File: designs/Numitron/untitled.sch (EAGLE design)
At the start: 10 parts, among them IC2 TLC5916IN, IC3 TLC5916IN, IC4 TLC5916IN, IC5 TLC5916IN

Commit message: added designs Numitron modular first finish review tomorrow or tuesday
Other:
- moved on the sheet: 1, 2, 3, 4, IC2, IC3, IC4, IC5, R1, SV1

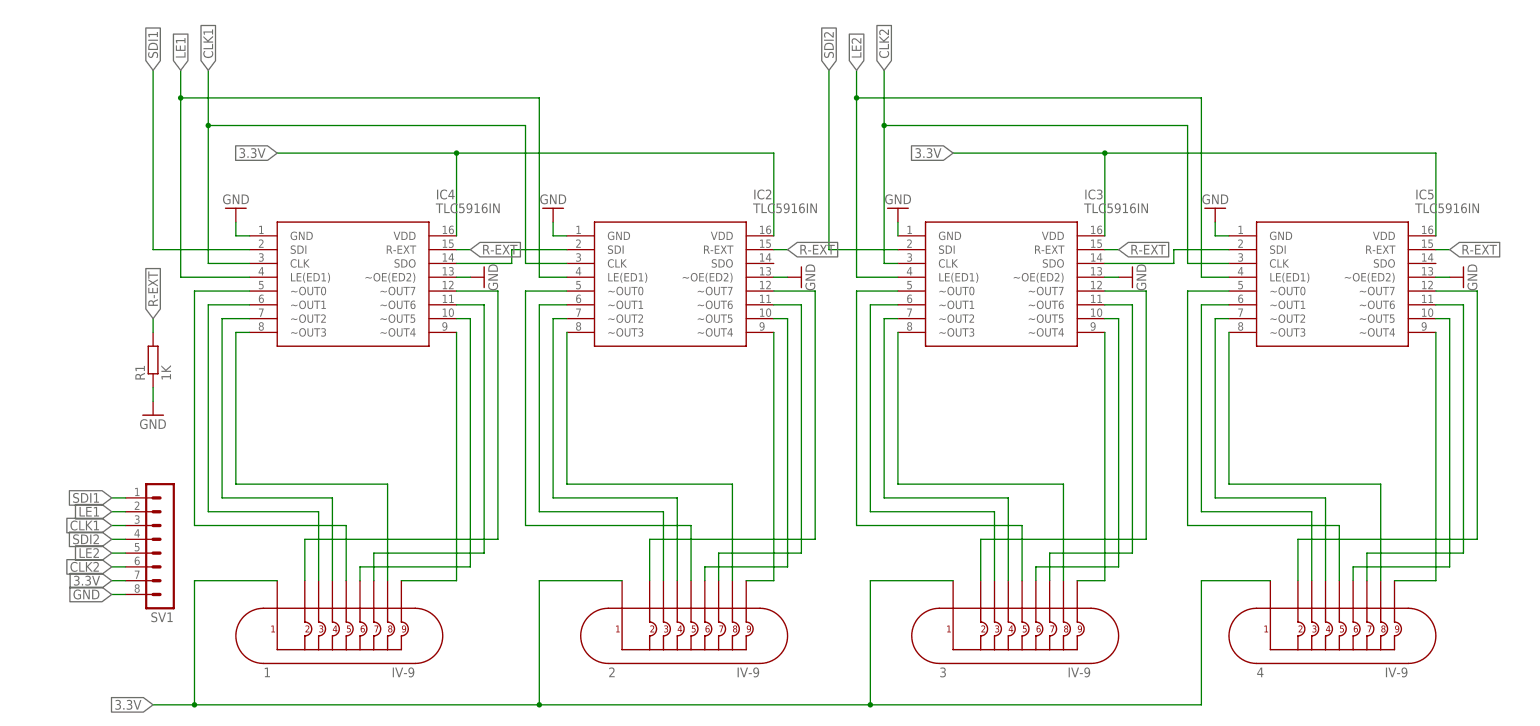
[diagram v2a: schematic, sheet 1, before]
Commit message: numitron 4 resistor error correction
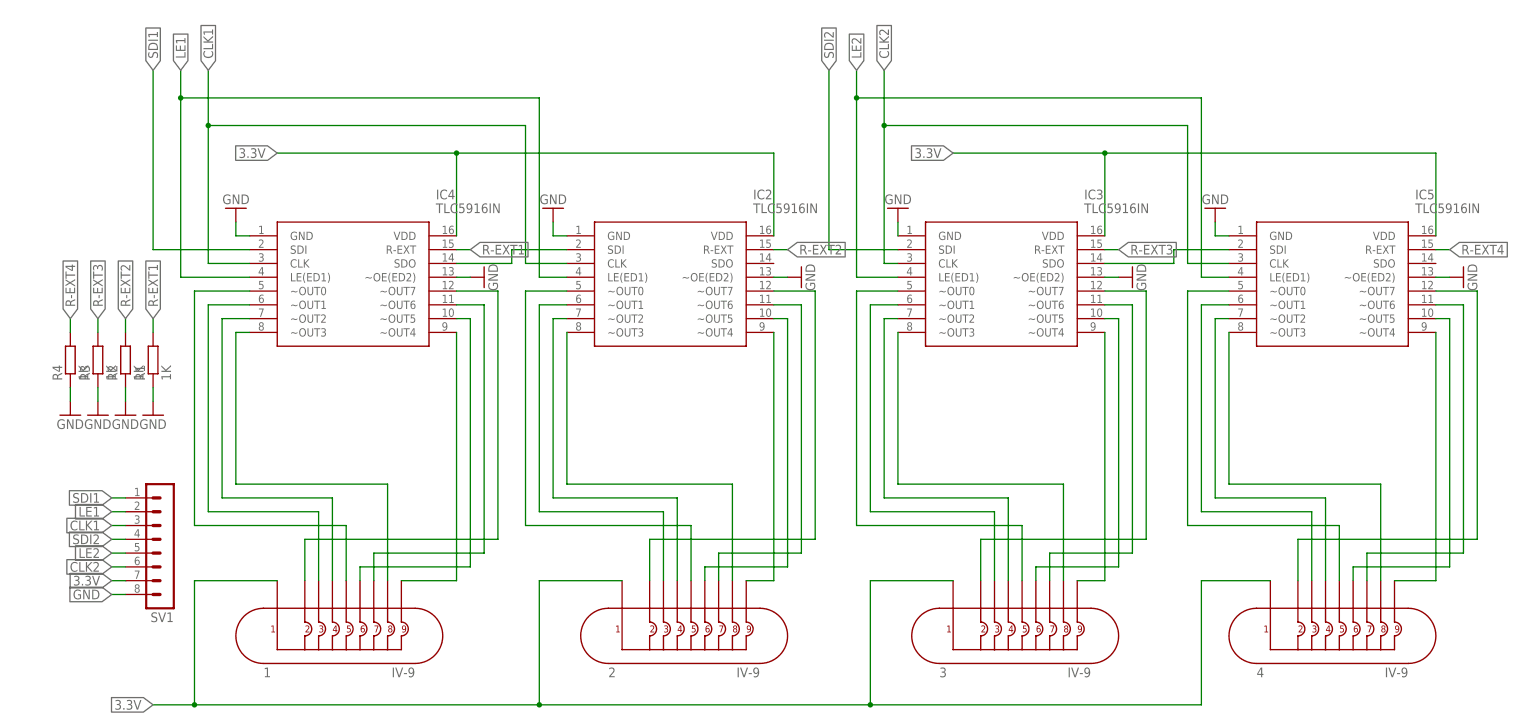
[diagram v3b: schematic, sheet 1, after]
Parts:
- added R2, R3, R4: 1K, rcl:R-EU_R1206
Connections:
- removed net R-EXT: IC2.R-EXT, IC3.R-EXT, IC4.R-EXT, IC5.R-EXT, R1.2
- new net R-EXT1: IC4.R-EXT, R1.2
- new net R-EXT2: IC2.R-EXT, R2.2
- new net R-EXT3: IC3.R-EXT, R3.2
- new net R-EXT4: IC5.R-EXT, R4.2
- net GND: now also R2.1, R3.1, R4.1
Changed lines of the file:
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@@
 <?xml version="1.0" encoding="utf-8"?>
 <!DOCTYPE eagle SYSTEM "eagle.dtd">
-<eagle version="9.5.1">
+<eagle version="9.4.2">
 <drawing>
 <settings>
@@
 <part name="GND12" library="supply1" library_urn="urn:adsk.eagle:library:371" deviceset="GND" device=""/>
 <part name="SV1" library="con-lstb" library_urn="urn:adsk.eagle:library:162" deviceset="MA08-1" device="" package3d_urn="urn:adsk.eagle:package:8343/1"/>
+<part name="R2" library="rcl" library_urn="urn:adsk.eagle:library:334" deviceset="R-EU_" device="R1206" package3d_urn="urn:adsk.eagle:package:23540/2" value="1K"/>
+<part name="GND9" library="supply1" library_urn="urn:adsk.eagle:library:371" deviceset="GND" device=""/>
+<part name="R3" library="rcl" library_urn="urn:adsk.eagle:library:334" deviceset="R-EU_" device="R1206" package3d_urn="urn:adsk.eagle:package:23540/2" value="1K"/>
+<part name="GND10" library="supply1" library_urn="urn:adsk.eagle:library:371" deviceset="GND" device=""/>
+<part name="R4" library="rcl" library_urn="urn:adsk.eagle:library:334" deviceset="R-EU_" device="R1206" package3d_urn="urn:adsk.eagle:package:23540/2" value="1K"/>
+<part name="GND11" library="supply1" library_urn="urn:adsk.eagle:library:371" deviceset="GND" device=""/>
 </parts>
 <sheets>
@@
 <attribute name="NAME" x="26.67" y="29.718" size="1.778" layer="95" rot="R180"/>
 </instance>
+<instance part="R2" gate="G$1" x="17.78" y="76.2" smashed="yes" rot="R90">
+<attribute name="NAME" x="16.2814" y="72.39" size="1.778" layer="95" rot="R90"/>
+<attribute name="VALUE" x="21.082" y="72.39" size="1.778" layer="96" rot="R90"/>
+</instance>
+<instance part="GND9" gate="1" x="17.78" y="66.04" smashed="yes">
+<attribute name="VALUE" x="15.24" y="63.5" size="1.778" layer="96"/>
+</instance>
+<instance part="R3" gate="G$1" x="12.7" y="76.2" smashed="yes" rot="R90">
+<attribute name="NAME" x="11.2014" y="72.39" size="1.778" layer="95" rot="R90"/>
+<attribute name="VALUE" x="16.002" y="72.39" size="1.778" layer="96" rot="R90"/>
+</instance>
+<instance part="GND10" gate="1" x="12.7" y="66.04" smashed="yes">
+<attribute name="VALUE" x="10.16" y="63.5" size="1.778" layer="96"/>
+</instance>
+<instance part="R4" gate="G$1" x="7.62" y="76.2" smashed="yes" rot="R90">
+<attribute name="NAME" x="6.1214" y="72.39" size="1.778" layer="95" rot="R90"/>
+<attribute name="VALUE" x="10.922" y="72.39" size="1.778" layer="96" rot="R90"/>
+</instance>
+<instance part="GND11" gate="1" x="7.62" y="66.04" smashed="yes">
+<attribute name="VALUE" x="5.08" y="63.5" size="1.778" layer="96"/>
+</instance>
 </instances>
 <busses>
@@
 <wire x1="17.78" y1="33.02" x2="15.24" y2="33.02" width="0.1524" layer="91"/>
 <label x="15.24" y="33.02" size="1.778" layer="95" rot="R180" xref="yes"/>
+</segment>
+<segment>
+<pinref part="R2" gate="G$1" pin="1"/>
+<wire x1="17.78" y1="71.12" x2="17.78" y2="68.58" width="0.1524" layer="91"/>
+<pinref part="GND9" gate="1" pin="GND"/>
+</segment>
+<segment>
+<pinref part="R3" gate="G$1" pin="1"/>
+<wire x1="12.7" y1="71.12" x2="12.7" y2="68.58" width="0.1524" layer="91"/>
+<pinref part="GND10" gate="1" pin="GND"/>
+</segment>
+<segment>
+<pinref part="R4" gate="G$1" pin="1"/>
+<wire x1="7.62" y1="71.12" x2="7.62" y2="68.58" width="0.1524" layer="91"/>
+<pinref part="GND11" gate="1" pin="GND"/>
 </segment>
 </net>
@@
 </segment>
 </net>
-<net name="R-EXT" class="0">
+<net name="R-EXT4" class="0">
+<segment>
+<pinref part="R4" gate="G$1" pin="2"/>
+<wire x1="7.62" y1="81.28" x2="7.62" y2="83.82" width="0.1524" layer="91"/>
+<label x="7.62" y="83.82" size="1.778" layer="95" rot="R90" xref="yes"/>
+</segment>
+<segment>
+<pinref part="IC5" gate="G$1" pin="R-EXT"/>
+<wire x1="259.08" y1="96.52" x2="261.62" y2="96.52" width="0.1524" layer="91"/>
+<label x="261.62" y="96.52" size="1.778" layer="95" xref="yes"/>
+</segment>
+</net>
+<net name="R-EXT3" class="0">
+<segment>
+<pinref part="R3" gate="G$1" pin="2"/>
+<wire x1="12.7" y1="81.28" x2="12.7" y2="83.82" width="0.1524" layer="91"/>
+<label x="12.7" y="83.82" size="1.778" layer="95" rot="R90" xref="yes"/>
+</segment>
+<segment>
+<pinref part="IC3" gate="G$1" pin="R-EXT"/>
+<wire x1="198.12" y1="96.52" x2="200.66" y2="96.52" width="0.1524" layer="91"/>
+<label x="200.66" y="96.52" size="1.778" layer="95" xref="yes"/>
+</segment>
+</net>
+<net name="R-EXT2" class="0">
+<segment>
+<pinref part="R2" gate="G$1" pin="2"/>
+<wire x1="17.78" y1="81.28" x2="17.78" y2="83.82" width="0.1524" layer="91"/>
+<label x="17.78" y="83.82" size="1.778" layer="95" rot="R90" xref="yes"/>
+</segment>
+<segment>
+<pinref part="IC2" gate="G$1" pin="R-EXT"/>
+<wire x1="137.16" y1="96.52" x2="139.7" y2="96.52" width="0.1524" layer="91"/>
+<label x="139.7" y="96.52" size="1.778" layer="95" xref="yes"/>
+</segment>
+</net>
+<net name="R-EXT1" class="0">
+<segment>
+<pinref part="R1" gate="G$1" pin="2"/>
+<wire x1="22.86" y1="81.28" x2="22.86" y2="83.82" width="0.1524" layer="91"/>
+<label x="22.86" y="83.82" size="1.778" layer="95" rot="R90" xref="yes"/>
+</segment>
 <segment>
 <pinref part="IC4" gate="G$1" pin="R-EXT"/>
@@
 <label x="81.28" y="96.52" size="1.778" layer="95" xref="yes"/>
 </segment>
-<segment>
-<pinref part="IC2" gate="G$1" pin="R-EXT"/>
-<wire x1="137.16" y1="96.52" x2="139.7" y2="96.52" width="0.1524" layer="91"/>
-<label x="139.7" y="96.52" size="1.778" layer="95" xref="yes"/>
-</segment>
-<segment>
-<pinref part="IC3" gate="G$1" pin="R-EXT"/>
-<wire x1="198.12" y1="96.52" x2="200.66" y2="96.52" width="0.1524" layer="91"/>
-<label x="200.66" y="96.52" size="1.778" layer="95" xref="yes"/>
-</segment>
-<segment>
-<pinref part="IC5" gate="G$1" pin="R-EXT"/>
-<wire x1="259.08" y1="96.52" x2="261.62" y2="96.52" width="0.1524" layer="91"/>
-<label x="261.62" y="96.52" size="1.778" layer="95" xref="yes"/>
-</segment>
-<segment>
-<pinref part="R1" gate="G$1" pin="2"/>
-<wire x1="22.86" y1="81.28" x2="22.86" y2="83.82" width="0.1524" layer="91"/>
-<label x="22.86" y="83.82" size="1.778" layer="95" rot="R90" xref="yes"/>
-</segment>
-</net>
+</net>
